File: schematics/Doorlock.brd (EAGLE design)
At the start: 65 x 56 mm, 45 parts, among them IC1 AT90S2313S, J1 RJ45, K1 G5V1, K2 G5V1, X1 RASPI_BOARD_B+#_H, X2 RIA182-04, X4 RIA182-05

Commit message: schematics: board: minor fixes
Credits go to Noby for the review!

Signed-off-by: Ralf Ramsauer <ralf@binary-kitchen.de>
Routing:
- net VCC: track 115.4 -> 100.7 mm
- net GND: track 254.8 -> 253.6 mm
- net +5V: track 86.8 -> 86.1 mm
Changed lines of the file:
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@@
 <board>
 <plain>
-<text x="37.1475" y="16.1925" size="1.27" layer="21" rot="R270">©Binary Kitchen e.V.
+<text x="40.79875" y="0.3175" size="1.27" layer="21" font="fixed" rot="R90">©Binary Kitchen e.V.
 Ralf Ramsauer</text>
 </plain>
@@
 <wire x1="40.2742" y1="37.4142" x2="40.64" y2="37.4142" width="0.4064" layer="1"/>
 <wire x1="28.69" y1="45.605" x2="28.69" y2="51.23" width="0.4064" layer="16"/>
-<wire x1="28.69" y1="48.375" x2="28.69" y2="51.23" width="0.4064" layer="1"/>
-<wire x1="19.84375" y1="48.26" x2="28.575" y2="48.26" width="0.4064" layer="1"/>
-<wire x1="28.575" y1="48.26" x2="28.69" y2="48.375" width="0.4064" layer="1"/>
+<wire x1="28.69" y1="51.23" x2="28.69" y2="49.2125" width="0.4064" layer="1"/>
 <wire x1="60.9575" y1="19.05" x2="60.9575" y2="16.51" width="0.254" layer="1"/>
 <wire x1="60.9575" y1="16.51" x2="60.9575" y2="13.97" width="0.254" layer="1"/>
-<wire x1="62.07125" y1="42.2275" x2="38.1" y2="42.2275" width="0.254" layer="1"/>
-<via x="38.1" y="42.2275" extent="1-16" drill="0.35"/>
-<wire x1="38.1" y1="42.2275" x2="38.1" y2="38.1" width="0.254" layer="16"/>
-<wire x1="38.1" y1="38.1" x2="37.1475" y2="37.1475" width="0.254" layer="16"/>
-<wire x1="62.07125" y1="42.2275" x2="64.29375" y2="40.005" width="0.254" layer="1"/>
-<wire x1="64.29375" y1="40.005" x2="64.29375" y2="22.70125" width="0.254" layer="1"/>
-<wire x1="64.29375" y1="22.70125" x2="60.9575" y2="19.365" width="0.254" layer="1"/>
-<wire x1="60.9575" y1="19.365" x2="60.9575" y2="19.05" width="0.254" layer="1"/>
+<wire x1="37.7825" y1="36.5125" x2="59.53125" y2="36.5125" width="0.254" layer="16"/>
 <wire x1="13.335" y1="46.3525" x2="15.71625" y2="46.3525" width="0.1524" layer="16"/>
 <wire x1="15.71625" y1="46.3525" x2="17.93625" y2="46.3525" width="0.1524" layer="16"/>
@@
 <wire x1="19.84375" y1="48.26" x2="9.68375" y2="48.26" width="0.4064" layer="16"/>
 <wire x1="9.68375" y1="48.26" x2="8.37" y2="49.57375" width="0.4064" layer="16"/>
+<wire x1="37.1475" y1="37.1475" x2="37.7825" y2="36.5125" width="0.254" layer="16"/>
+<via x="60.96" y="21.74875" extent="1-16" drill="0.35"/>
+<wire x1="60.96" y1="21.74875" x2="60.96" y2="19.0525" width="0.254" layer="1"/>
+<wire x1="60.96" y1="19.0525" x2="60.9575" y2="19.05" width="0.254" layer="1"/>
+<wire x1="59.53125" y1="36.5125" x2="60.96" y2="35.08375" width="0.254" layer="16"/>
+<wire x1="60.96" y1="35.08375" x2="60.96" y2="21.74875" width="0.254" layer="16"/>
+<wire x1="28.69" y1="49.2125" x2="27.7375" y2="48.26" width="0.4064" layer="1"/>
+<wire x1="27.7375" y1="48.26" x2="19.84375" y2="48.26" width="0.4064" layer="1"/>
 </signal>
 <signal name="GND">
@@
 <wire x1="14.7454" y1="52.4746" x2="16.50553125" y2="52.4746" width="0.3048" layer="1"/>
 <wire x1="61.595" y1="31.43" x2="61.595" y2="35.88" width="0.4064" layer="1"/>
-<wire x1="52.07" y1="27.8892" x2="55.5117" y2="24.4475" width="0.4064" layer="1"/>
-<wire x1="55.5117" y1="24.4475" x2="63.5" y2="24.4475" width="0.4064" layer="1"/>
-<wire x1="63.5" y1="24.4475" x2="63.5" y2="30.1625" width="0.4064" layer="1"/>
+<wire x1="55.03545" y1="24.92375" x2="52.07" y2="27.8892" width="0.4064" layer="1"/>
 <wire x1="63.5" y1="30.1625" x2="62.2325" y2="31.43" width="0.4064" layer="1"/>
 <wire x1="62.2325" y1="31.43" x2="61.595" y2="31.43" width="0.4064" layer="1"/>
@@
 <wire x1="40.0025" y1="33.6575" x2="38.4175" y2="33.6575" width="0.254" layer="1"/>
 <wire x1="52.07" y1="17.30375" x2="52.07" y2="27.8892" width="0.254" layer="1"/>
+<wire x1="63.5" y1="30.1625" x2="63.5" y2="25.7175" width="0.4064" layer="1"/>
+<wire x1="63.5" y1="25.7175" x2="62.70625" y2="24.92375" width="0.4064" layer="1"/>
+<wire x1="62.70625" y1="24.92375" x2="55.03545" y2="24.92375" width="0.4064" layer="1"/>
 </signal>
 <signal name="N$6">
@@
 <wire x1="45.415" y1="11.1125" x2="46.20875" y2="10.31875" width="0.254" layer="1"/>
 <wire x1="46.20875" y1="10.31875" x2="51.59375" y2="10.31875" width="0.254" layer="1"/>
-<wire x1="41.5925" y1="22.5425" x2="45.72" y2="26.67" width="0.254" layer="1"/>
-<wire x1="45.72" y1="26.67" x2="46.6725" y2="26.67" width="0.254" layer="1"/>
-<wire x1="46.6725" y1="26.67" x2="46.99" y2="26.9875" width="0.254" layer="1"/>
+<wire x1="41.5925" y1="22.5425" x2="45.87875" y2="26.82875" width="0.254" layer="1"/>
+<wire x1="45.87875" y1="26.82875" x2="46.83125" y2="26.82875" width="0.254" layer="1"/>
+<wire x1="46.83125" y1="26.82875" x2="46.99" y2="26.9875" width="0.254" layer="1"/>
 <wire x1="46.99" y1="26.9875" x2="46.99" y2="27.8892" width="0.254" layer="1"/>
 </signal>
@@
 <wire x1="46.51375" y1="10.795" x2="46.51375" y2="11.27125" width="0.254" layer="16"/>
 <wire x1="58.26125" y1="8.255" x2="49.05375" y2="8.255" width="0.254" layer="16"/>
-<wire x1="46.51375" y1="11.27125" x2="46.51375" y2="11.7134125" width="0.254" layer="1"/>
+<wire x1="46.51375" y1="11.27125" x2="46.51375" y2="11.5546625" width="0.254" layer="1"/>
 <wire x1="60.6425" y1="15.40125" x2="59.53375" y2="15.40125" width="0.1524" layer="16"/>
 <wire x1="59.53375" y1="15.40125" x2="59.3725" y2="15.24" width="0.1524" layer="16"/>
@@
 <wire x1="59.3725" y1="15.24" x2="59.3725" y2="14.285" width="0.1524" layer="1"/>
 <wire x1="59.3725" y1="14.285" x2="59.0575" y2="13.97" width="0.1524" layer="1"/>
-<wire x1="46.51375" y1="11.7134125" x2="42.2275" y2="15.9996625" width="0.254" layer="1"/>
-<wire x1="42.2275" y1="15.9996625" x2="42.2275" y2="22.06625" width="0.254" layer="1"/>
+<wire x1="46.51375" y1="11.5546625" x2="42.2275" y2="15.8409125" width="0.254" layer="1"/>
+<wire x1="42.2275" y1="15.8409125" x2="42.2275" y2="22.06625" width="0.254" layer="1"/>
 <wire x1="42.2275" y1="22.06625" x2="46.355" y2="26.19375" width="0.254" layer="1"/>
 <wire x1="47.625" y1="26.19375" x2="48.26" y2="26.82875" width="0.254" layer="1"/>
@@
 <wire x1="26.67" y1="17.145" x2="19.685" y2="17.145" width="0.635" layer="1"/>
 <wire x1="19.685" y1="17.145" x2="17.78" y2="15.24" width="0.635" layer="1"/>
-<wire x1="8.37" y1="53.77" x2="10.91" y2="53.77" width="0.635" layer="16"/>
-<wire x1="6.399" y1="51.29919375" x2="6.35" y2="51.25019375" width="1.016" layer="16"/>
-<wire x1="6.399" y1="51.29919375" x2="6.399" y2="52.705" width="1.016" layer="16"/>
-<wire x1="6.399" y1="52.705" x2="8.37" y2="53.77" width="1.016" layer="16"/>
 <contactref element="K1" pad="2"/>
 <wire x1="27.94" y1="24.87" x2="27.2" y2="24.87" width="0.508" layer="1"/>
@@
 <via x="12.85875" y="36.35375" extent="1-16" drill="1.5"/>
 <wire x1="12.85875" y1="36.35375" x2="17.3475" y2="36.35375" width="1.016" layer="1"/>
-<wire x1="6.35" y1="51.25019375" x2="6.35" y2="36.35375" width="1.016" layer="16"/>
-<wire x1="6.35" y1="36.35375" x2="12.85875" y2="36.35375" width="1.016" layer="16"/>
+<wire x1="7.46125" y1="36.35375" x2="12.85875" y2="36.35375" width="1.016" layer="16"/>
 <wire x1="17.62125" y1="36.35375" x2="17.3475" y2="36.35375" width="1.27" layer="1"/>
+<wire x1="7.46125" y1="36.35375" x2="6.35" y2="37.465" width="1.016" layer="16"/>
+<wire x1="6.35" y1="52.22875" x2="7.89125" y2="53.77" width="1.016" layer="16"/>
+<wire x1="7.89125" y1="53.77" x2="8.37" y2="53.77" width="1.016" layer="16"/>
+<wire x1="6.35" y1="37.465" x2="6.35" y2="52.22875" width="1.016" layer="16"/>
+<wire x1="8.37" y1="53.77" x2="10.91" y2="53.77" width="1.016" layer="16"/>
 </signal>
 <signal name="GND2">

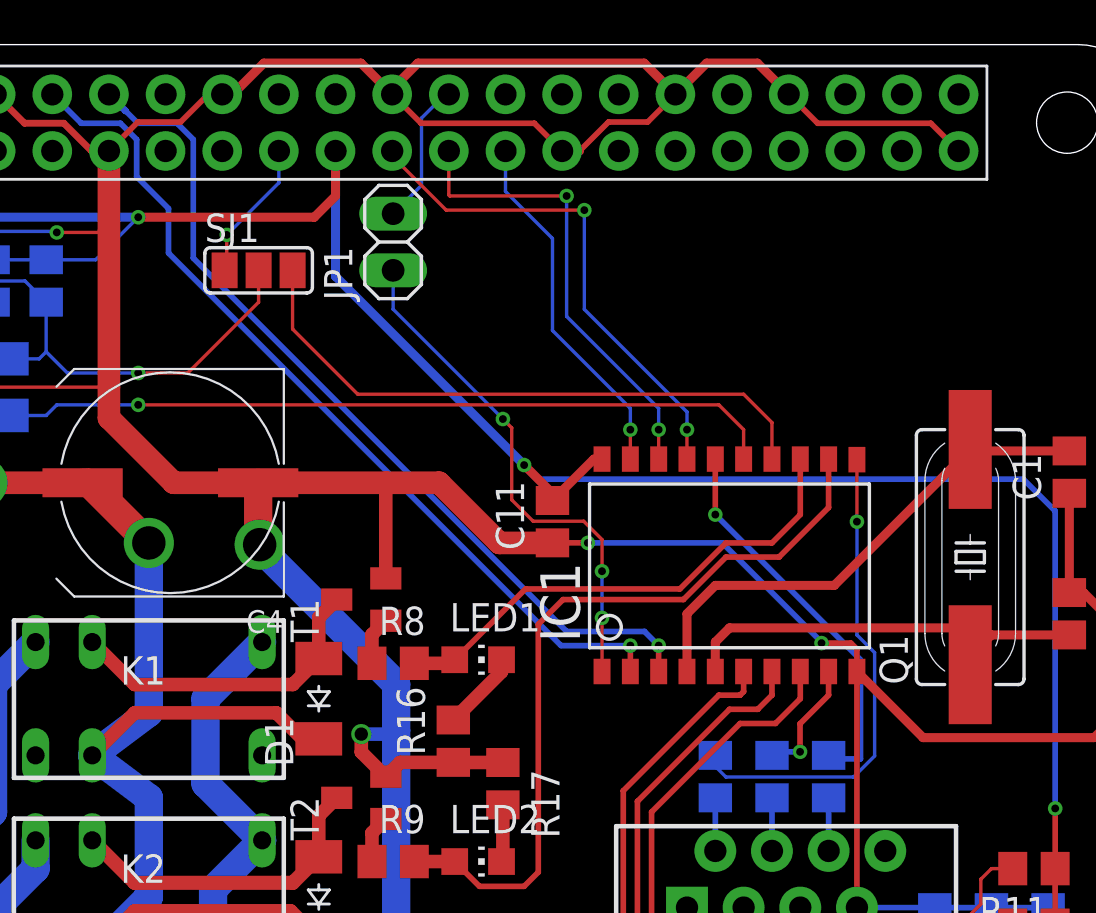
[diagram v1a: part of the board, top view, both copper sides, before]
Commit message: schematics: add Raspberry Pi Hat EEPROM
Signed-off-by: Ralf Ramsauer <ralf@binary-kitchen.de>
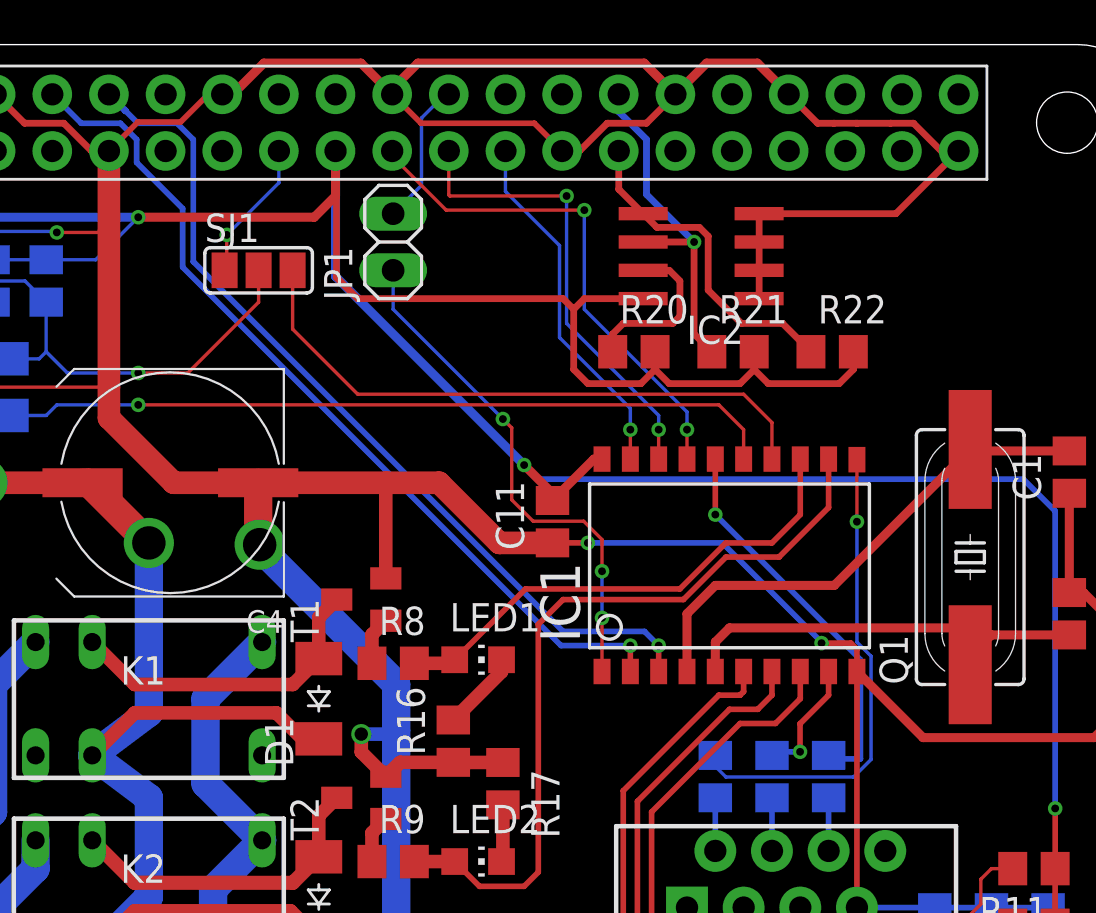
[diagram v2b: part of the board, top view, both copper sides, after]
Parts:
- added IC2: 24C32ASN, microchip:SO-08
- added R20, R21, R22: 3k9, rcl:R0805
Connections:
- new net ID_SC: IC2.6, R21.1, X1.28
- new net ID_SD: IC2.5, R22.1, X1.27
- new net ID_WP: IC2.7, R20.1
- net GND: now also IC2.1, IC2.2, IC2.3, IC2.4
- net VCC: now also IC2.8, R20.2, R21.2, R22.2
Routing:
- net VCC: track 100.7 -> 138.9 mm
- net ID_SC: track 0.00 -> 15.6 mm, vias 0 -> 1
- net ID_SD: track 0.00 -> 14.8 mm
- net GND: track 253.6 -> 267.9 mm
- net ID_WP: track 0.00 -> 7.57 mm

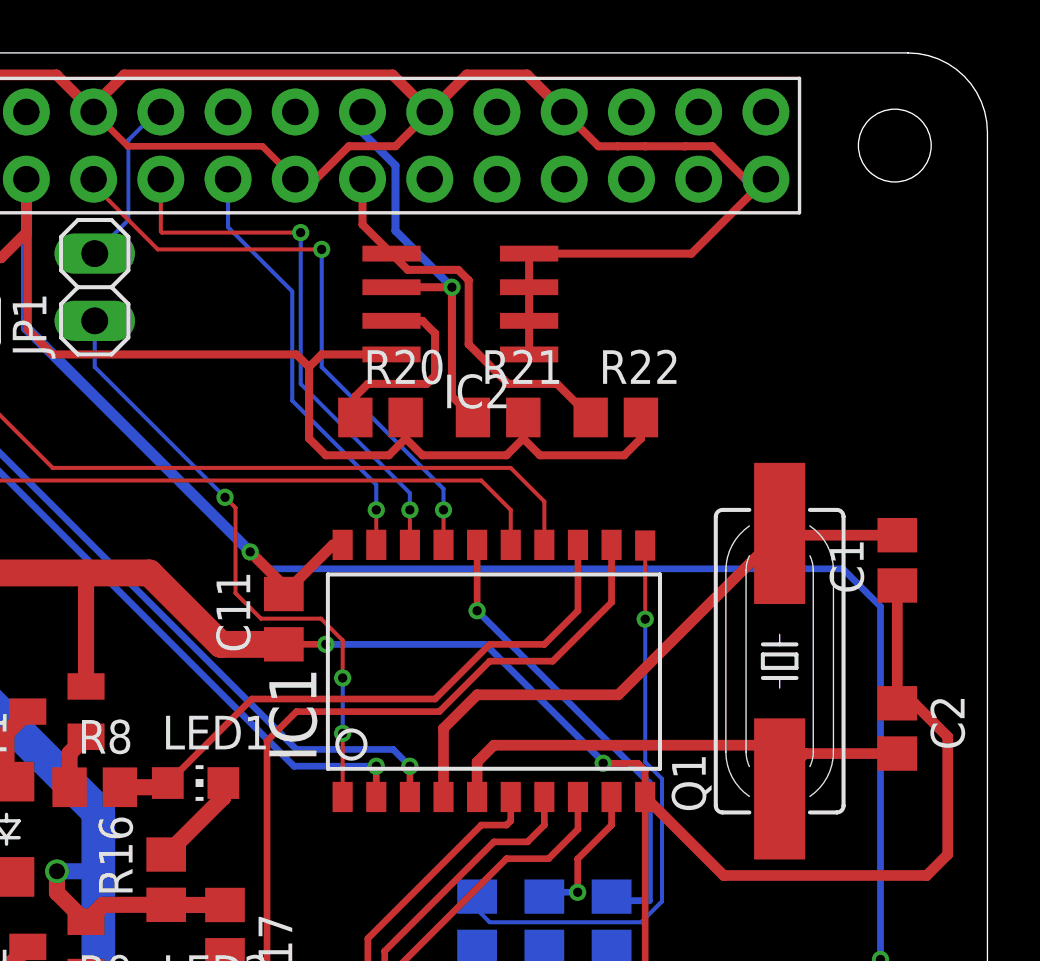
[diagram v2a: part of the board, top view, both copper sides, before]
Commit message: schematics: board: minor fixups
Signed-off-by: Ralf Ramsauer <ralf@binary-kitchen.de>
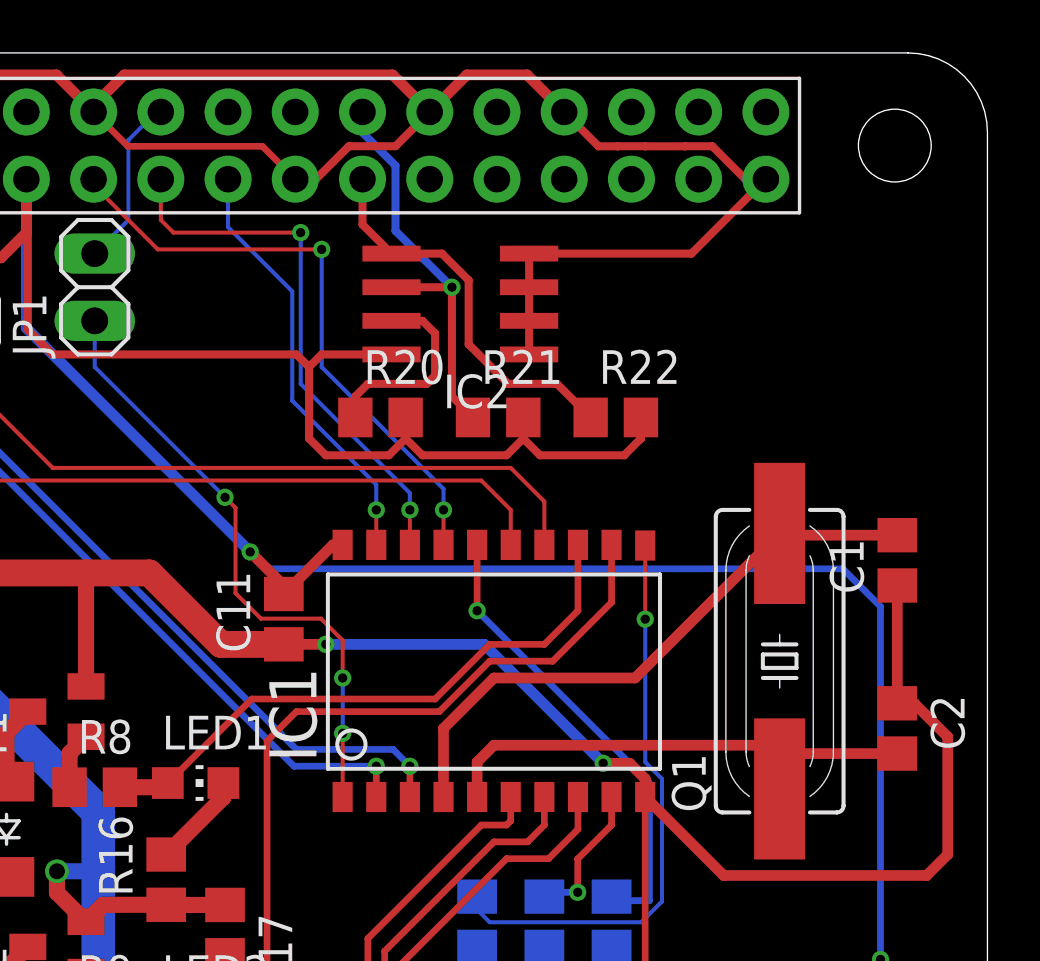
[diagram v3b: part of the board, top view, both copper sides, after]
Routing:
- net GND: track 267.9 -> 267.4 mm
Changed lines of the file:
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@@
 <wire x1="25.4767125" y1="55.17095" x2="29.82905" y2="55.17095" width="0.4064" layer="1"/>
 <wire x1="29.82905" y1="55.17095" x2="31.23" y2="53.77" width="0.4064" layer="1"/>
-<wire x1="43.93" y1="53.77" x2="43.92875" y2="53.77125" width="0.4064" layer="1"/>
-<wire x1="43.92875" y1="53.77125" x2="42.52905" y2="55.17095" width="0.4064" layer="1"/>
+<wire x1="43.93" y1="53.77" x2="42.52905" y2="55.17095" width="0.4064" layer="1"/>
 <wire x1="42.52905" y1="55.17095" x2="32.385" y2="55.17095" width="0.4064" layer="1"/>
 <wire x1="31.23" y1="54.01595" x2="32.385" y2="55.17095" width="0.4064" layer="1"/>
@@
 <wire x1="30.945" y1="36.3425" x2="30.95625" y2="36.35375" width="0.6096" layer="1"/>
 <via x="40.0025" y="33.6575" extent="1-16" drill="0.35"/>
-<wire x1="40.0025" y1="33.6575" x2="46.035" y2="33.6575" width="0.254" layer="16"/>
-<wire x1="46.035" y1="33.6575" x2="50.4825" y2="29.21" width="0.254" layer="16"/>
-<wire x1="50.4825" y1="29.21" x2="50.4825" y2="29.162" width="0.254" layer="16"/>
 <via x="50.4825" y="29.162" extent="1-16" drill="0.35"/>
-<wire x1="50.4825" y1="29.162" x2="51.8005" y2="29.162" width="0.254" layer="1"/>
-<wire x1="51.8005" y1="29.162" x2="52.07" y2="28.8925" width="0.254" layer="1"/>
-<wire x1="52.07" y1="28.8925" x2="52.07" y2="27.8892" width="0.254" layer="1"/>
 <wire x1="31.41" y1="25.24125" x2="31.41" y2="7.28" width="1.27" layer="16"/>
 <wire x1="31.41" y1="7.28" x2="29.21" y2="5.08" width="1.27" layer="16"/>
 <via x="29.21" y="5.08" extent="1-16" drill="1.5"/>
-<wire x1="40.0025" y1="33.6575" x2="38.4175" y2="33.6575" width="0.254" layer="1"/>
 <wire x1="52.07" y1="17.30375" x2="52.07" y2="27.8892" width="0.254" layer="1"/>
 <wire x1="63.5" y1="30.1625" x2="63.5" y2="25.7175" width="0.4064" layer="1"/>
@@
 <contactref element="IC2" pad="3"/>
 <contactref element="IC2" pad="4"/>
-<wire x1="47.685" y1="47.14875" x2="47.685" y2="47.3075" width="0.1524" layer="1"/>
-<wire x1="47.685" y1="47.14875" x2="47.685" y2="47.3075" width="0.254" layer="1"/>
 <wire x1="47.685" y1="44.60875" x2="47.685" y2="45.87875" width="0.3048" layer="1"/>
 <wire x1="47.685" y1="45.87875" x2="47.685" y2="47.14875" width="0.3048" layer="1"/>
@@
 <wire x1="42.6346" y1="52.4746" x2="40.87446875" y2="52.4746" width="0.3048" layer="1"/>
 <wire x1="40.87446875" y1="52.4746" x2="39.62986875" y2="51.23" width="0.3048" layer="1"/>
+<wire x1="38.4175" y1="33.6575" x2="40.0025" y2="33.6575" width="0.4064" layer="1"/>
+<wire x1="50.4825" y1="29.162" x2="45.987" y2="33.6575" width="0.4064" layer="16"/>
+<wire x1="45.987" y1="33.6575" x2="40.0025" y2="33.6575" width="0.4064" layer="16"/>
+<wire x1="52.07" y1="27.8892" x2="52.07" y2="28.575" width="0.4064" layer="1"/>
+<wire x1="51.483" y1="29.162" x2="50.4825" y2="29.162" width="0.4064" layer="1"/>
+<wire x1="52.07" y1="28.575" x2="51.483" y2="29.162" width="0.4064" layer="1"/>
 </signal>
 <signal name="N$6">
@@
 <contactref element="C1" pad="2"/>
 <wire x1="57.15" y1="37.846" x2="57.084" y2="37.78" width="0.4064" layer="1"/>
-<wire x1="56.9595" y1="37.6555" x2="51.054" y2="31.75" width="0.4064" layer="1"/>
-<wire x1="45.72" y1="31.75" x2="44.45" y2="30.48" width="0.4064" layer="1"/>
+<wire x1="56.9595" y1="37.6555" x2="51.689" y2="32.385" width="0.4064" layer="1"/>
+<wire x1="46.355" y1="32.385" x2="44.45" y2="30.48" width="0.4064" layer="1"/>
 <wire x1="44.45" y1="30.48" x2="44.45" y2="27.8892" width="0.4064" layer="1"/>
-<wire x1="51.054" y1="31.75" x2="45.72" y2="31.75" width="0.4064" layer="1"/>
+<wire x1="51.689" y1="32.385" x2="46.355" y2="32.385" width="0.4064" layer="1"/>
 <wire x1="61.595" y1="37.78" x2="57.084" y2="37.78" width="0.4064" layer="1"/>
 <wire x1="57.084" y1="37.78" x2="56.9595" y2="37.6555" width="0.4064" layer="1"/>
@@
 <wire x1="45.72" y1="29.21" x2="46.355" y2="29.845" width="0.4064" layer="1"/>
 <wire x1="46.355" y1="29.845" x2="57.15" y2="29.845" width="0.4064" layer="1"/>
-<wire x1="57.15" y1="29.845" x2="57.15" y2="28.575" width="0.4064" layer="1"/>
-<wire x1="57.15" y1="28.575" x2="57.15" y2="28.194" width="0.4064" layer="1"/>
-<wire x1="61.595" y1="29.53" x2="58.105" y2="29.53" width="0.4064" layer="1"/>
-<wire x1="58.105" y1="29.53" x2="57.15" y2="28.575" width="0.4064" layer="1"/>
+<wire x1="61.595" y1="29.53" x2="57.465" y2="29.53" width="0.4064" layer="1"/>
+<wire x1="57.465" y1="29.53" x2="57.15" y2="29.845" width="0.4064" layer="1"/>
+<wire x1="57.15" y1="28.194" x2="57.15" y2="29.845" width="0.4064" layer="1"/>
 </signal>
 <signal name="+12V">
@@
 <wire x1="43.18" y1="39.37" x2="39.0525" y2="43.4975" width="0.1524" layer="16"/>
 <via x="39.0525" y="49.2125" extent="1-16" drill="0.35"/>
-<wire x1="39.0525" y1="49.2125" x2="33.81375" y2="49.2125" width="0.1524" layer="1"/>
-<wire x1="33.77" y1="49.25625" x2="33.77" y2="51.23" width="0.1524" layer="1"/>
-<wire x1="33.81375" y1="49.2125" x2="33.77" y2="49.25625" width="0.1524" layer="1"/>
+<wire x1="33.77" y1="51.23" x2="33.77" y2="49.68875" width="0.1524" layer="1"/>
+<wire x1="33.77" y1="49.68875" x2="34.24625" y2="49.2125" width="0.1524" layer="1"/>
+<wire x1="34.24625" y1="49.2125" x2="39.0525" y2="49.2125" width="0.1524" layer="1"/>
 </signal>
 <signal name="SCK">
@@
 <wire x1="41.39" y1="49.51375" x2="41.39" y2="51.23" width="0.3048" layer="1"/>
 <contactref element="R22" pad="1"/>
-<wire x1="42.485" y1="48.41875" x2="43.0994" y2="47.80435" width="0.3048" layer="1"/>
-<wire x1="43.0994" y1="47.80435" x2="45.00596875" y2="47.80435" width="0.3048" layer="1"/>
-<wire x1="45.00596875" y1="47.80435" x2="45.3997" y2="47.41061875" width="0.3048" layer="1"/>
 <wire x1="45.3997" y1="44.99115625" x2="46.89335625" y2="43.4975" width="0.3048" layer="1"/>
 <wire x1="45.3997" y1="47.41061875" x2="45.3997" y2="44.99115625" width="0.3048" layer="1"/>
 <wire x1="48.73875" y1="43.4975" x2="50.00875" y2="42.2275" width="0.3048" layer="1"/>
 <wire x1="46.89335625" y1="43.4975" x2="48.73875" y2="43.4975" width="0.3048" layer="1"/>
+<wire x1="42.485" y1="48.41875" x2="44.39156875" y2="48.41875" width="0.3048" layer="1"/>
+<wire x1="44.39156875" y1="48.41875" x2="45.3997" y2="47.41061875" width="0.3048" layer="1"/>
 </signal>
 <signal name="ID_SC">
